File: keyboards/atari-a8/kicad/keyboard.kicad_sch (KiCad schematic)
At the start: 140 parts, among them SW200 ESC, SW201 1, SW202 2, SW203 3, SW204 4, SW205 5, SW206 6, SW207 7, SW208 8, SW209 9, SW210 0, SW211 LT, SW212 GT, SW213 BS, SW214 C_UP, SW215 C_LEFT, SW216 C_DOWN, SW217 C_RIGHT, SW218 TAB, SW219 Q, SW220 W, SW221 E, SW222 R, SW223 T, SW224 Y, SW225 U, SW226 I, SW227 O, SW228 P, SW229 DASH, SW230 EQUAL, SW231 RETURN, SW232 HELP, SW233 RESET, SW234 OPTION, SW235 SELECT, SW236 CONTROL, SW237 A, SW238 S, SW239 D, SW240 F, SW241 G, SW242 H, SW243 J, SW244 K, SW245 L, SW246 SEMI, SW247 PLUS, SW248 ASTRIX, SW249 CAPS, SW250 START, SW251 POWER, SW252 MENU, SW253 TURBO, SW254 FN, SW255 LSHIFT, SW256 Z, SW257 X, SW258 C, SW259 V, SW260 B, SW261 N, SW262 M, SW263 COMMA, SW264 PERIOD, SW265 SLASH, SW266 RSHIFT, SW267 INV, SW268 BREAK, SW269 SPACE

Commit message: Correct key sizes placed, diodes located, various auto-drawn stuff removed from PCB
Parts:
- SW200, SW232, SW233, SW234, SW235, SW249, SW250, SW251, SW252, SW253, SW267, SW268: footprint mx_alps:MX-1U -> mx_alps:MX-1.25U
- SW213, SW236: footprint mx_alps:MX-1U -> mx_alps:MX-2U
- SW218, SW266: footprint mx_alps:MX-1U -> mx_alps:MX-1.75U
- SW231: footprint mx_alps:MX-1U -> mx_alps:MX-1.5U
- SW255: footprint mx_alps:MX-1U -> mx_alps:MX-2.25U
- SW269: footprint mx_alps:MX-1U -> mx_alps:MX-6.25U

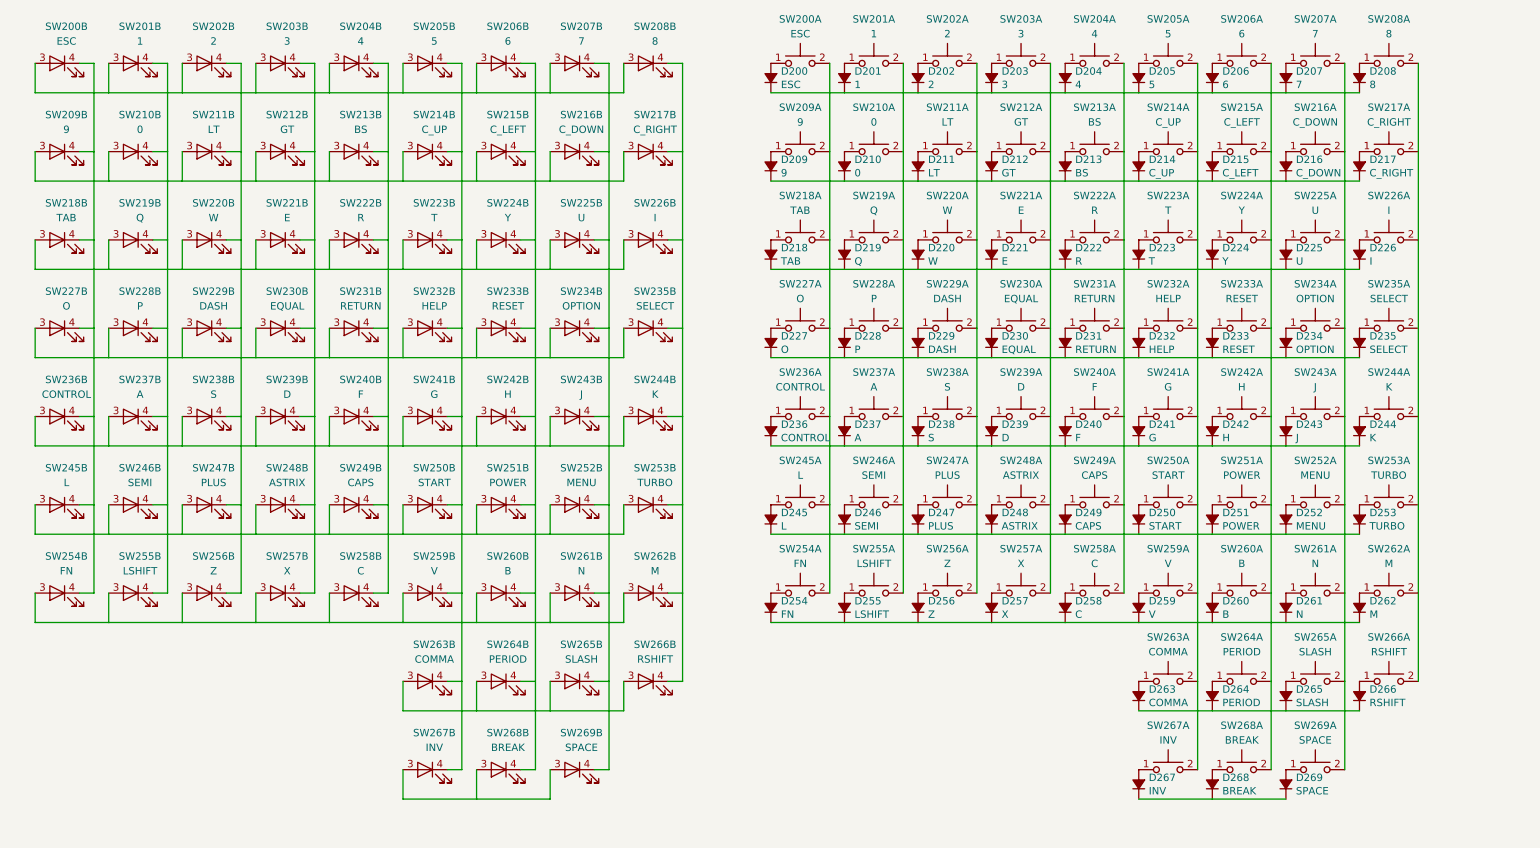
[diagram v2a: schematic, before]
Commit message: All global labels rendered. MAX7219's added. PCB updaed
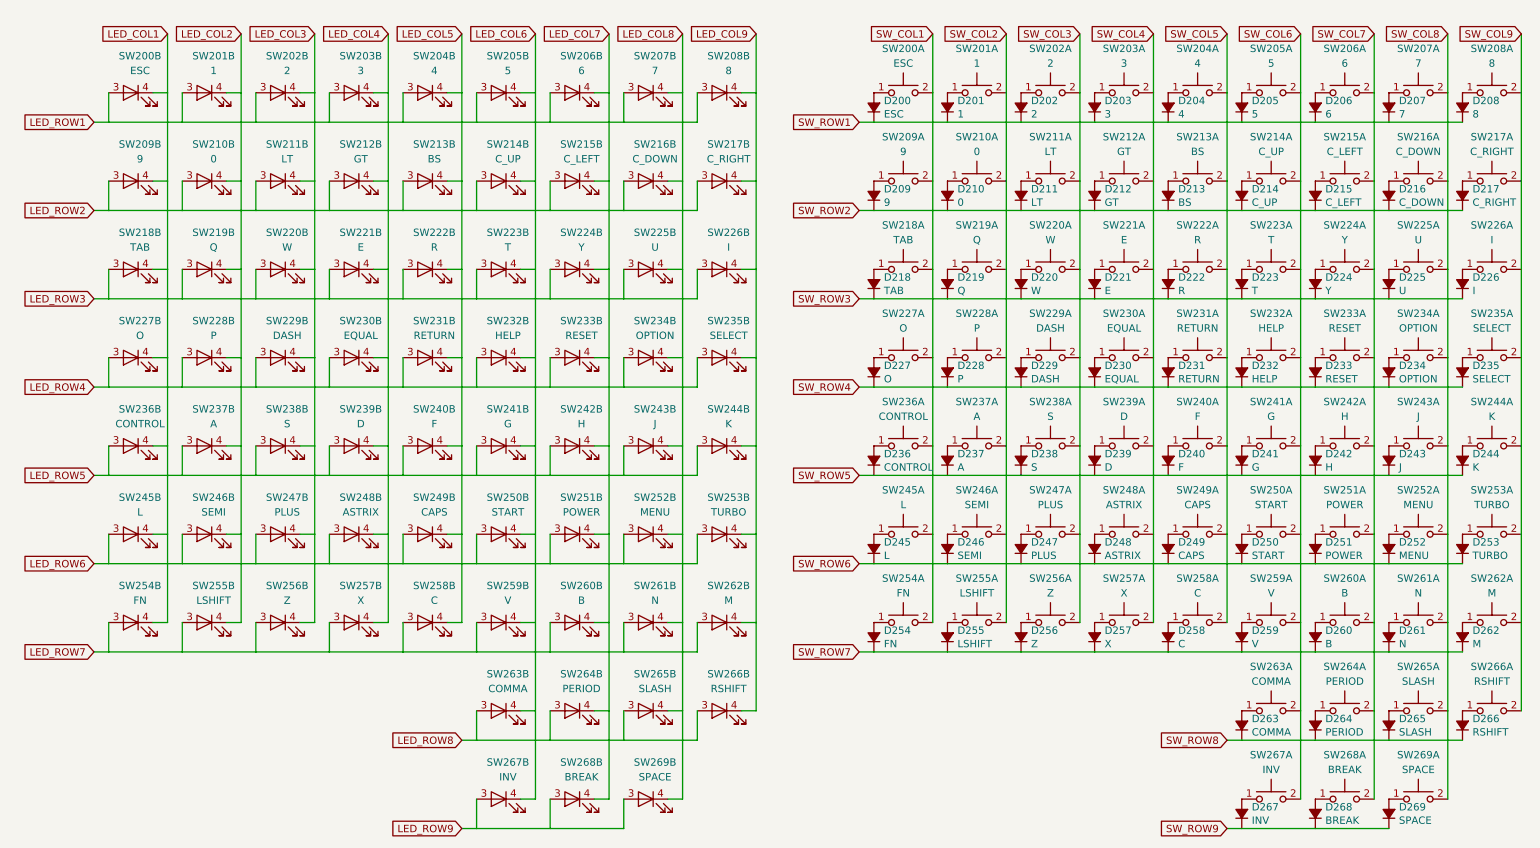
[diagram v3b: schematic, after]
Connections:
- net SW_ROW2: now reaches D209.1 (K), D210.1 (K), D211.1 (K), D212.1 (K), D213.1 (K), D214.1 (K), D215.1 (K), D216.1 (K), D217.1 (K)
- net SW_ROW1: now reaches D200.1 (K), D201.1 (K), D202.1 (K), D203.1 (K), D204.1 (K), D205.1 (K), D206.1 (K), D207.1 (K), D208.1 (K)
- net SW_ROW5: now reaches D236.1 (K), D237.1 (K), D238.1 (K), D239.1 (K), D240.1 (K), D241.1 (K), D242.1 (K), D243.1 (K), D244.1 (K)
- net SW_ROW7: now reaches D254.1 (K), D255.1 (K), D256.1 (K), D257.1 (K), D258.1 (K), D259.1 (K), D260.1 (K), D261.1 (K), D262.1 (K)
- net SW_ROW9: now reaches D267.1 (K), D268.1 (K), D269.1 (K)
- net SW_ROW3: now reaches D218.1 (K), D219.1 (K), D220.1 (K), D221.1 (K), D222.1 (K), D223.1 (K), D224.1 (K), D225.1 (K), D226.1 (K)
- net SW_ROW4: now reaches D227.1 (K), D228.1 (K), D229.1 (K), D230.1 (K), D231.1 (K), D232.1 (K), D233.1 (K), D234.1 (K), D235.1 (K)
- net SW_ROW6: now reaches D245.1 (K), D246.1 (K), D247.1 (K), D248.1 (K), D249.1 (K), D250.1 (K), D251.1 (K), D252.1 (K), D253.1 (K)
- net SW_ROW8: now reaches D263.1 (K), D264.1 (K), D265.1 (K), D266.1 (K)
- net LED_ROW1: now reaches SW200.3, SW201.3, SW202.3, SW203.3, SW204.3, SW205.3, SW206.3, SW207.3, SW208.3
- net LED_COL1: now reaches SW200.4, SW209.4, SW218.4, SW227.4, SW236.4, SW245.4, SW254.4
- net LED_COL2: now reaches SW201.4, SW210.4, SW219.4, SW228.4, SW237.4, SW246.4, SW255.4
- net LED_COL3: now reaches SW202.4, SW211.4, SW220.4, SW229.4, SW238.4, SW247.4, SW256.4
- net LED_COL4: now reaches SW203.4, SW212.4, SW221.4, SW230.4, SW239.4, SW248.4, SW257.4
- net LED_COL5: now reaches SW204.4, SW213.4, SW222.4, SW231.4, SW240.4, SW249.4, SW258.4
- net LED_COL6: now reaches SW205.4, SW214.4, SW223.4, SW232.4, SW241.4, SW250.4, SW259.4, SW263.4, SW267.4
- net LED_COL7: now reaches SW206.4, SW215.4, SW224.4, SW233.4, SW242.4, SW251.4, SW260.4, SW264.4, SW268.4
- net LED_COL8: now reaches SW207.4, SW216.4, SW225.4, SW234.4, SW243.4, SW252.4, SW261.4, SW265.4, SW269.4
- net LED_COL9: now reaches SW208.4, SW217.4, SW226.4, SW235.4, SW244.4, SW253.4, SW262.4, SW266.4
- net LED_ROW2: now reaches SW209.3, SW210.3, SW211.3, SW212.3, SW213.3, SW214.3, SW215.3, SW216.3, SW217.3
- net LED_ROW3: now reaches SW218.3, SW219.3, SW220.3, SW221.3, SW222.3, SW223.3, SW224.3, SW225.3, SW226.3
- net LED_ROW4: now reaches SW227.3, SW228.3, SW229.3, SW230.3, SW231.3, SW232.3, SW233.3, SW234.3, SW235.3
- net LED_ROW5: now reaches SW236.3, SW237.3, SW238.3, SW239.3, SW240.3, SW241.3, SW242.3, SW243.3, SW244.3
- net LED_ROW6: now reaches SW245.3, SW246.3, SW247.3, SW248.3, SW249.3, SW250.3, SW251.3, SW252.3, SW253.3
- net LED_ROW7: now reaches SW254.3, SW255.3, SW256.3, SW257.3, SW258.3, SW259.3, SW260.3, SW261.3, SW262.3
- net LED_ROW8: now reaches SW263.3, SW264.3, SW265.3, SW266.3
- net LED_ROW9: now reaches SW267.3, SW268.3, SW269.3
- net SW_COL1: now reaches SW200.2, SW209.2, SW218.2, SW227.2, SW236.2, SW245.2, SW254.2
- net SW_COL2: now reaches SW201.2, SW210.2, SW219.2, SW228.2, SW237.2, SW246.2, SW255.2
- net SW_COL3: now reaches SW202.2, SW211.2, SW220.2, SW229.2, SW238.2, SW247.2, SW256.2
- net SW_COL4: now reaches SW203.2, SW212.2, SW221.2, SW230.2, SW239.2, SW248.2, SW257.2
- net SW_COL5: now reaches SW204.2, SW213.2, SW222.2, SW231.2, SW240.2, SW249.2, SW258.2
- net SW_COL6: now reaches SW205.2, SW214.2, SW223.2, SW232.2, SW241.2, SW250.2, SW259.2, SW263.2, SW267.2
- net SW_COL7: now reaches SW206.2, SW215.2, SW224.2, SW233.2, SW242.2, SW251.2, SW260.2, SW264.2, SW268.2
- net SW_COL8: now reaches SW207.2, SW216.2, SW225.2, SW234.2, SW243.2, SW252.2, SW261.2, SW265.2, SW269.2
- net SW_COL9: now reaches SW208.2, SW217.2, SW226.2, SW235.2, SW244.2, SW253.2, SW262.2, SW266.2
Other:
- moved on the sheet: SW200A, SW200B, SW201A, SW201B, SW202A, SW202B, SW203A, SW203B, SW204A, SW204B, SW205A, SW205B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

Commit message: Changed LSHIFT from 2.25U to 2U (more available)
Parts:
- SW232: footprint mx_alps:MX-1.25U -> (none)
- SW255: footprint (none) -> mx_alps:MX-2U
- SW255: footprint mx_alps:MX-2.25U -> mx_alps:MX-2U
